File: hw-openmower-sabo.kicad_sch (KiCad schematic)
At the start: 20 parts, among them J1 Conn_01x05_Pin, J20 Conn_01x02, J31 Conn_01x03_Pin, J32 Conn_02x08_Odd_Even, J33 Molex 470531000, M1 Fan, M2 Fan, Q4 BSS138, Q5 BSS138, U7 M24C02-WMN

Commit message: Update status
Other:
- note added: "--------------- DESIGN FAULTS -------------- 1. Front-Wheel & Top- Stop-Button Emergencies for Series-I: Outputs of OPAMPs (for Series-II) need to get cutted! U6 Pin1, 2 & 14 2. See required changes in RobotConnectorsSeries2"
- note removed: "--------------- DESIGN FAILURES -------------- 1. Front-Wheel & Top- Stop-Button Emergencies for Series-I: Outputs of OPAMPs (for Series-II) need to get cutted! U6 Pin1, 2 & 14"
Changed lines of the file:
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@@
 		)
 	)
-	(text "--------------- DESIGN FAILURES --------------\n\n1. Front-Wheel & Top- Stop-Button Emergencies for Series-I:\n   Outputs of OPAMPs (for Series-II) need to get cutted!\n   U6 Pin1, 2 & 14"
+	(text "--------------- DESIGN FAULTS --------------\n\n1. Front-Wheel & Top- Stop-Button Emergencies for Series-I:\n   Outputs of OPAMPs (for Series-II) need to get cutted!\n   U6 Pin1, 2 & 14\n2. See required changes in RobotConnectorsSeries2"
 		(exclude_from_sim no)
 		(at 24.638 87.122 0)

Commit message: Prepare v0.2
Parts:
- added C88: 100nF@50V, Capacitor_SMD:C_0402_1005Metric, symbol Device:C
- added R36: 0.1, Resistor_SMD:R_1206_3216Metric, symbol Device:R
- added R37: 27k, Resistor_SMD:R_0603_1608Metric_Pad0.98x0.95mm_HandSolder, symbol Device:R
- added R38: 22k, Resistor_SMD:R_0603_1608Metric_Pad0.98x0.95mm_HandSolder, symbol Device:R
- added U44: INA180A1, Package_TO_SOT_SMD:SOT-23-5, symbol Amplifier_Current:INA180A1
- J20: now fitted; now in the parts list
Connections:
- net 3.3V: now also C88.1, U44.5 (V+)
- net AGPIO2: now also U44.1
- net GND: now also C88.2, R37.2, U44.2 (GND)
- net VIN: now also R36.2, U44.4 (-); no longer D15.1 (K), D28.1 (K)
- new net: R37.1, R38.1, U44.3 (+)
- new net: D15.1 (K), D28.1 (K), R36.1, R38.2
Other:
- sheet RobotConnectors ports: added INP_~{CS}, LATCH_~{LOAD}, SPI_CLK, SPI_RX, SPI_TX, UI_S2_BTN_~{CS}, ~{OE}; removed LED_RX, LED_TX, UI_BTN_~{CE}, UI_LATCH_LOAD, UI_SPI_CLK, UI_SPI_RX, UI_SPI_TX, UI_~{OE}
- note added: "(PA8)"
- note added: "(PF7)"
- note removed: "--------------- DESIGN FAULTS -------------- 1. Front-Wheel & Top- Stop-Button Emergencies for Series-I: Outputs of OPAMPs (for Series-II) need to get cutted! U6 Pin1, 2 & 14 2. See required changes in RobotConnectorsSeries2"
- moved on the sheet: D15, D28

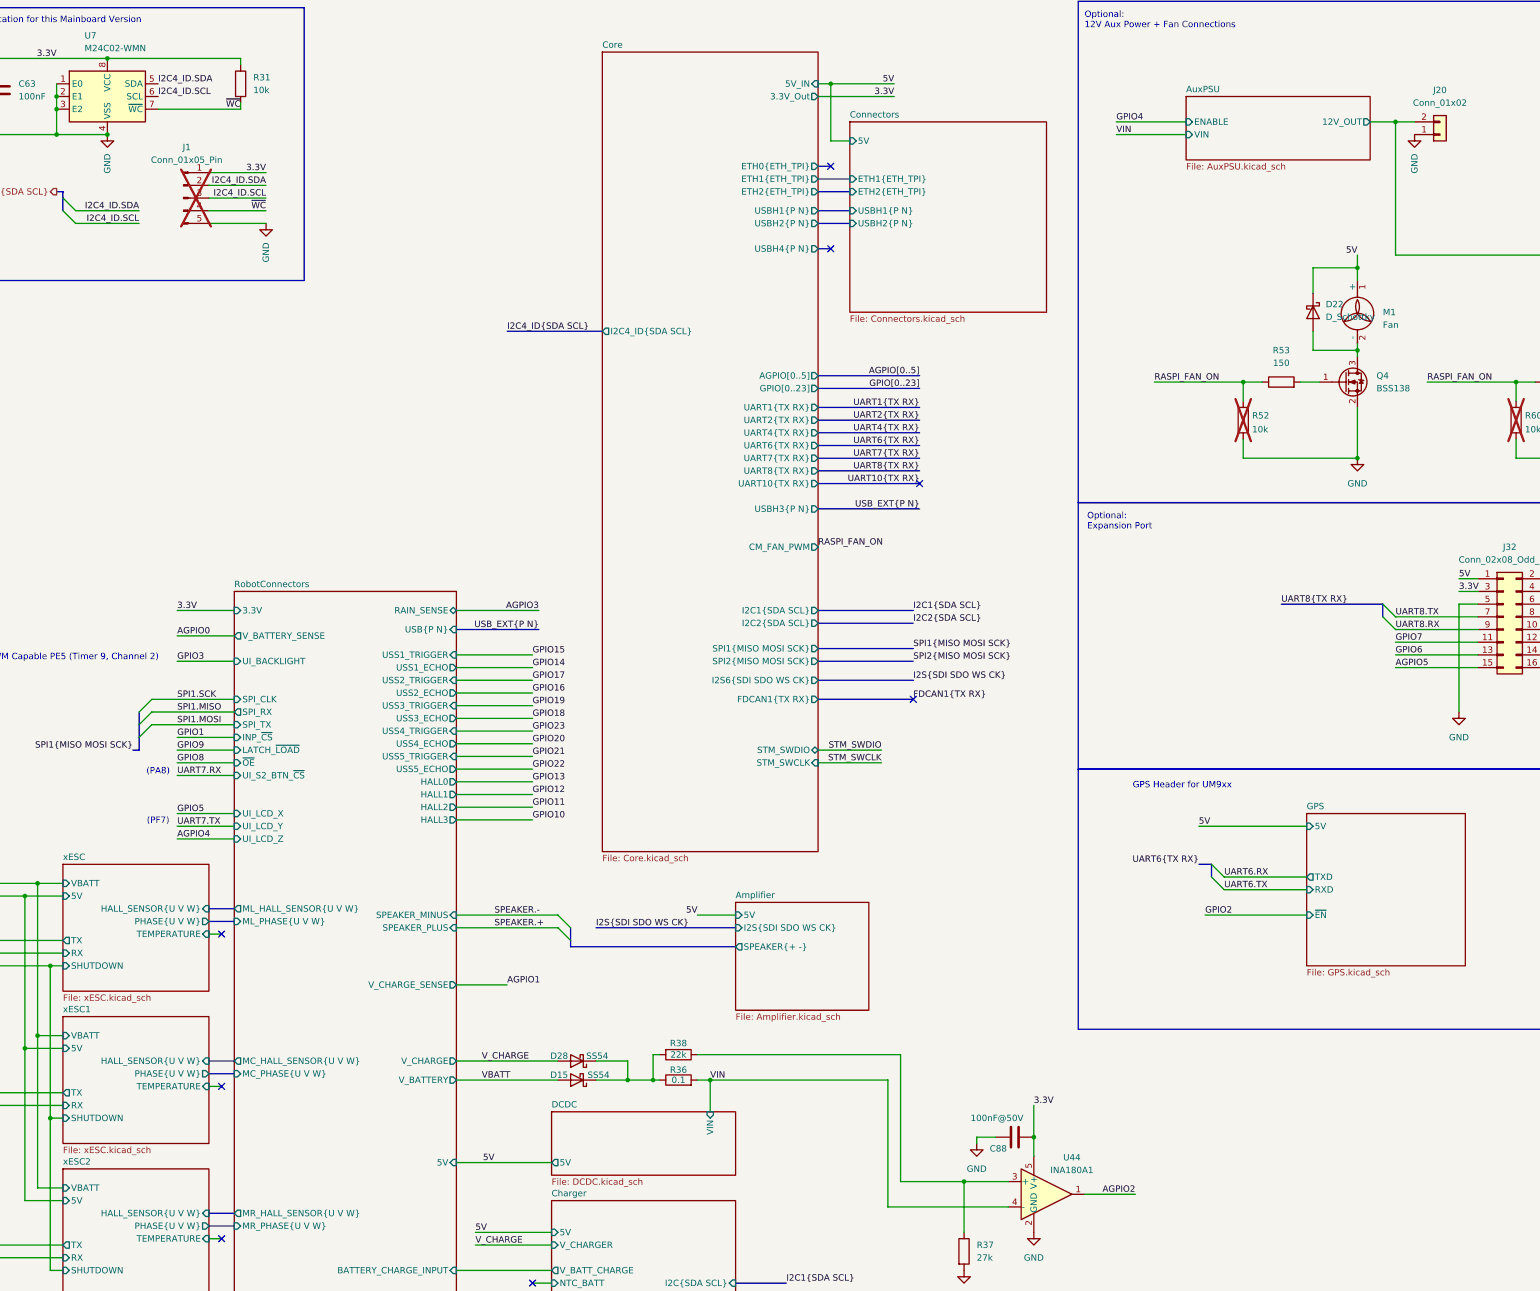
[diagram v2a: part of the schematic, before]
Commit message: Add RoHS Compliance Summary
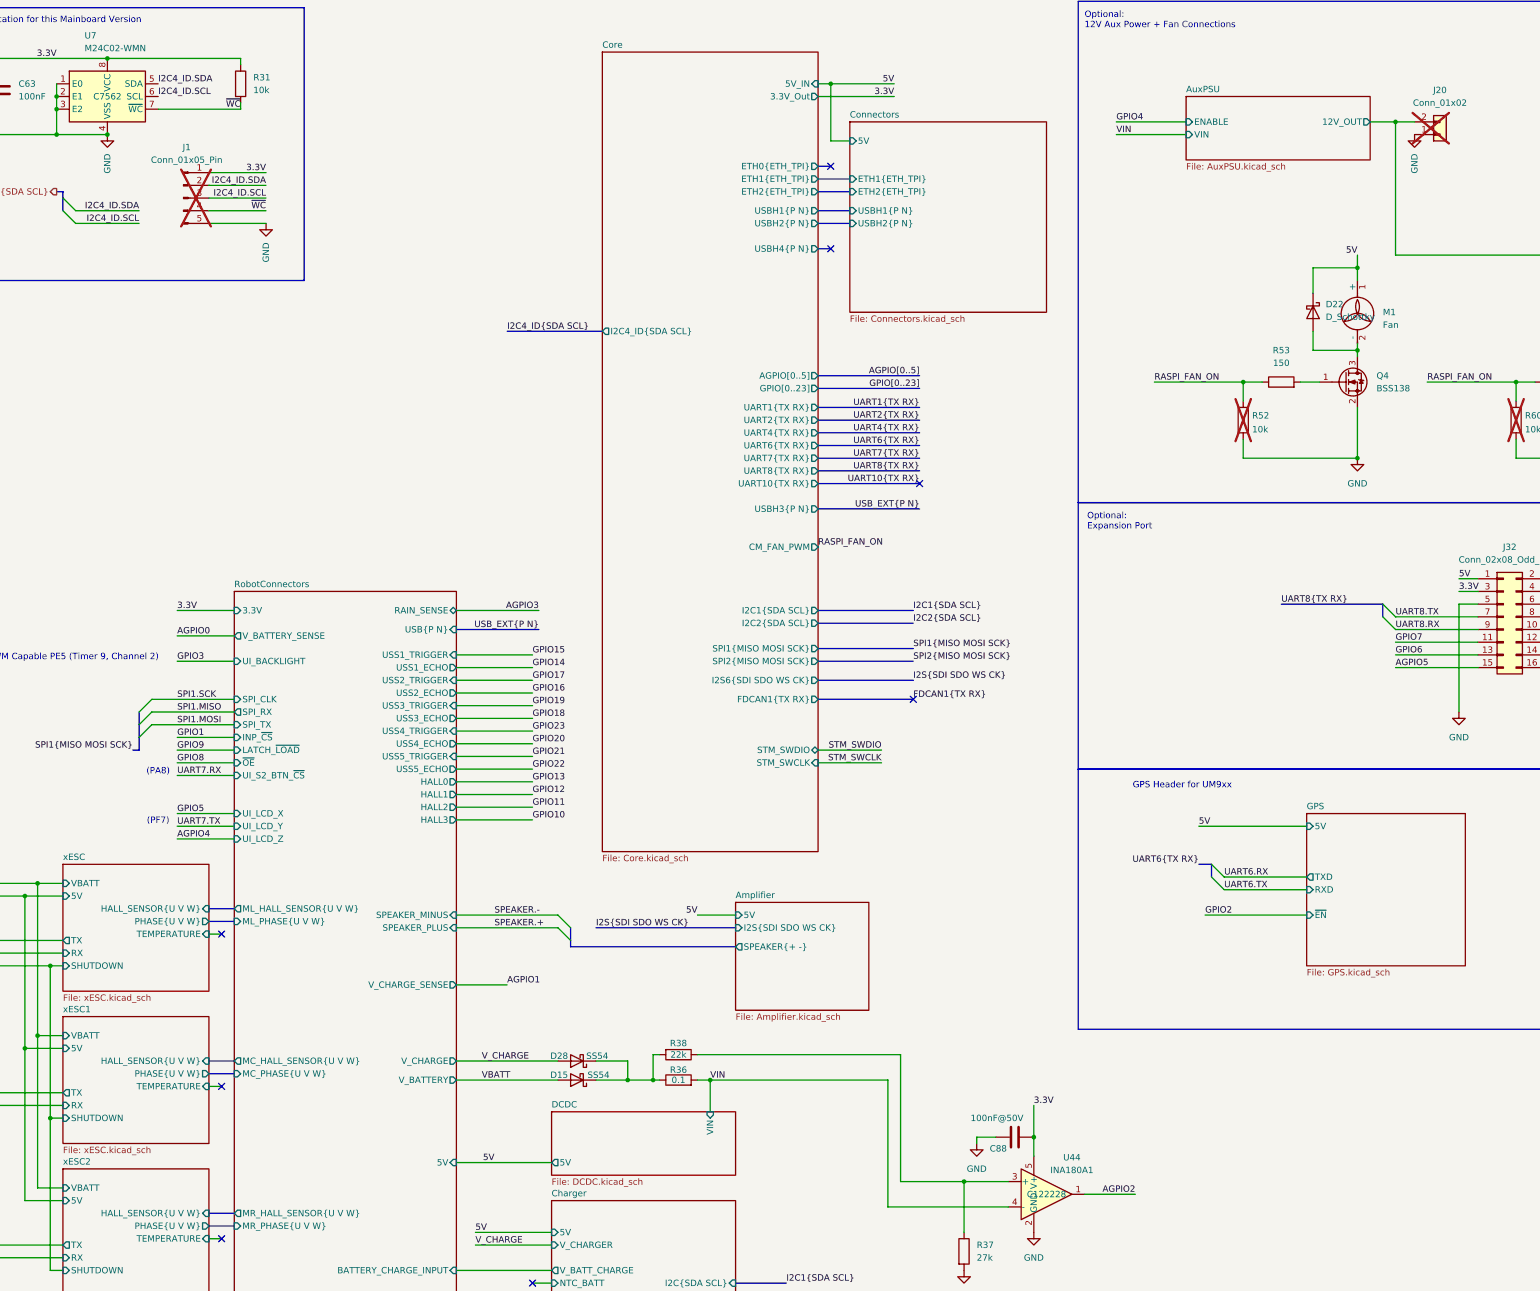
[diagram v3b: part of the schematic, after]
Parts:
- J20: now not fitted; now left out of the parts list
- U44: JLC C122228 -> (none); LCSC Part # (none) -> C122228
- U7: JLC C7562 -> (none); LCSC Part # (none) -> C7562
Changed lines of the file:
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@@
+			)
+		)
+		(property "MPN" ""
+			(at 161.29 224.79 0)
+			(effects
+				(font
+					(size 1.27 1.27)
+				)
 			)
 		)
@@
 			)
 		)
+		(property "MPN" ""
+			(at 326.39 137.16 0)
+			(effects
+				(font
+					(size 1.27 1.27)
+				)
+			)
+		)
 		(pin "9"
 		)
@@
 			)
 		)
+		(property "MPN" ""
+			(at 365.76 193.04 0)
+			(effects
+				(font
+					(size 1.27 1.27)
+				)
+			)
+		)
 		(pin "1"
 		)
@@
 			)
 		)
+		(property "MPN" ""
+			(at 351.79 77.47 0)
+			(effects
+				(font
+					(size 1.27 1.27)
+				)
+			)
+		)
 		(pin "1"
 		)
@@
 				)
 				(hide yes)
+			)
+		)
+		(property "MPN" ""
+			(at 140.97 226.06 0)
+			(effects
+				(font
+					(size 1.27 1.27)
+				)
 			)
 		)
@@
 			)
 		)
+		(property "MPN" ""
+			(at 349.25 90.17 0)
+			(effects
+				(font
+					(size 1.27 1.27)
+				)
+			)
+		)
 		(pin "1"
 		)
@@
 			)
 		)
+		(property "MPN" ""
+			(at 297.18 77.47 0)
+			(effects
+				(font
+					(size 1.27 1.27)
+				)
+			)
+		)
 		(pin "1"
 		)
@@
 			)
 		)
+		(property "MPN" ""
+			(at 274.32 97.79 0)
+			(effects
+				(font
+					(size 1.27 1.27)
+				)
+			)
+		)
 		(pin "1"
 		)
@@
 			)
 		)
+		(property "MPN" ""
+			(at 140.97 229.87 0)
+			(effects
+				(font
+					(size 1.27 1.27)
+				)
+			)
+		)
 		(pin "1"
 		)
@@
 			)
 		)
-		(property "JLC" "C7562"
+		(property "JLC" ""
 			(at 46.99 33.02 0)
 			(effects
@@
 				)
 				(hide yes)
+			)
+		)
+		(property "MPN" ""
+			(at 46.99 33.02 0)
+			(effects
+				(font
+					(size 1.27 1.27)
+				)
+			)
+		)
+		(property "LCSC Part #" "C7562"
+			(at 46.99 33.02 0)
+			(effects
+				(font
+					(size 1.27 1.27)
+				)
 			)
 		)
@@
 			)
 		)
+		(property "MPN" ""
+			(at 294.64 90.17 0)
+			(effects
+				(font
+					(size 1.27 1.27)
+				)
+			)
+		)
 		(pin "1"
 		)
@@
 			)
 		)
+		(property "MPN" ""
+			(at 73.66 30.48 0)
+			(effects
+				(font
+					(size 1.27 1.27)
+				)
+			)
+		)
 		(pin "2"
 		)
@@
 			)
 		)
-		(property "JLC" "C122228"
+		(property "JLC" ""
 			(at 234.95 252.73 0)
 			(effects
@@
 				)
 				(hide yes)
+			)
+		)
+		(property "MPN" ""
+			(at 234.95 252.73 0)
+			(effects
+				(font
+					(size 1.27 1.27)
+				)
+			)
+		)
+		(property "LCSC Part #" "C122228"
+			(at 234.95 252.73 0)
+			(effects
+				(font
+					(size 1.27 1.27)
+				)
 			)
 		)
@@
 			)
 		)
+		(property "MPN" ""
+			(at 218.44 264.16 0)
+			(effects
+				(font
+					(size 1.27 1.27)
+				)
+			)
+		)
 		(pin "2"
 		)
@@
 			)
 		)
+		(property "MPN" ""
+			(at 62.23 53.34 0)
+			(effects
+				(font
+					(size 1.27 1.27)
+				)
+			)
+		)
 		(pin "5"
 		)
@@
 			)
 		)
+		(property "MPN" ""
+			(at 342.9 76.2 0)
+			(effects
+				(font
+					(size 1.27 1.27)
+				)
+			)
+		)
 		(pin "1"
 		)
@@
 			)
 		)
+		(property "MPN" ""
+			(at 281.94 90.17 0)
+			(effects
+				(font
+					(size 1.27 1.27)
+				)
+			)
+		)
 		(pin "1"
 		)
@@
 			)
 		)
+		(property "MPN" ""
+			(at 336.55 90.17 0)
+			(effects
+				(font
+					(size 1.27 1.27)
+				)
+			)
+		)
 		(pin "1"
 		)
@@
 			)
 		)
+		(property "MPN" ""
+			(at 161.29 229.87 0)
+			(effects
+				(font
+					(size 1.27 1.27)
+				)
+			)
+		)
 		(pin "2"
 		)
@@
 		(unit 1)
 		(exclude_from_sim no)
-		(in_bom yes)
-		(on_board yes)
-		(dnp no)
+		(in_bom no)
+		(on_board yes)
+		(dnp yes)
 		(property "Reference" "J20"
 			(at 313.69 31.75 0)
@@
 				)
 				(hide yes)
+			)
+		)
+		(property "MPN" ""
+			(at 313.69 40.64 0)
+			(effects
+				(font
+					(size 1.27 1.27)
+				)
 			)
 		)
@@
 			)
 		)
+		(property "MPN" ""
+			(at 328.93 97.79 0)
+			(effects
+				(font
+					(size 1.27 1.27)
+				)
+			)
+		)
 		(pin "1"
 		)
@@
 			)
 		)
+		(property "MPN" ""
+			(at 288.29 76.2 0)
+			(effects
+				(font
+					(size 1.27 1.27)
+				)
+			)
+		)
 		(pin "1"
 		)
@@
 			)
 		)
+		(property "MPN" ""
+			(at 386.08 91.44 0)
+			(effects
+				(font
+					(size 1.27 1.27)
+				)
+			)
+		)
 		(pin "1"
 		)
@@
 				)
 				(hide yes)
+			)
+		)
+		(property "MPN" ""
+			(at 228.6 241.3 0)
+			(effects
+				(font
+					(size 1.27 1.27)
+				)
 			)
 		)
@@
 			)
 		)
+		(property "MPN" ""
+			(at 25.4 31.75 0)
+			(effects
+				(font
+					(size 1.27 1.27)
+				)
+			)
+		)

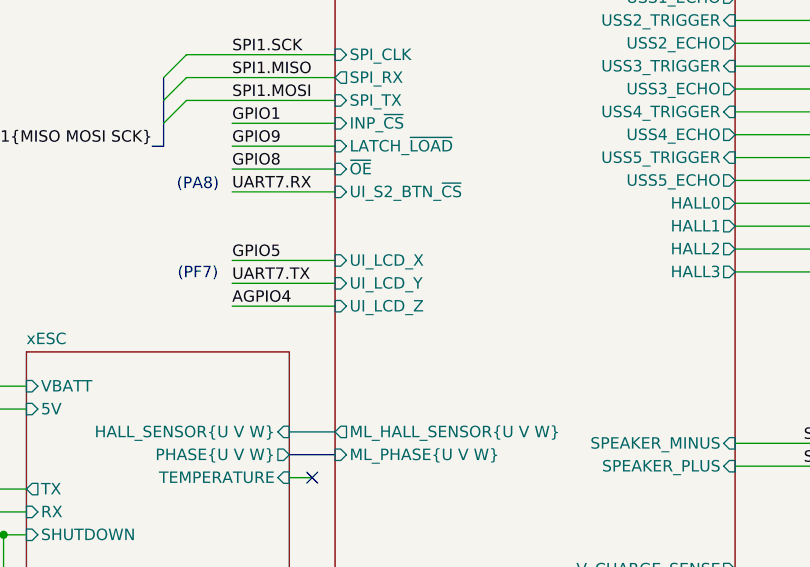
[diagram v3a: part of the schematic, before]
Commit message: Finish v0.2 schematic and ERC
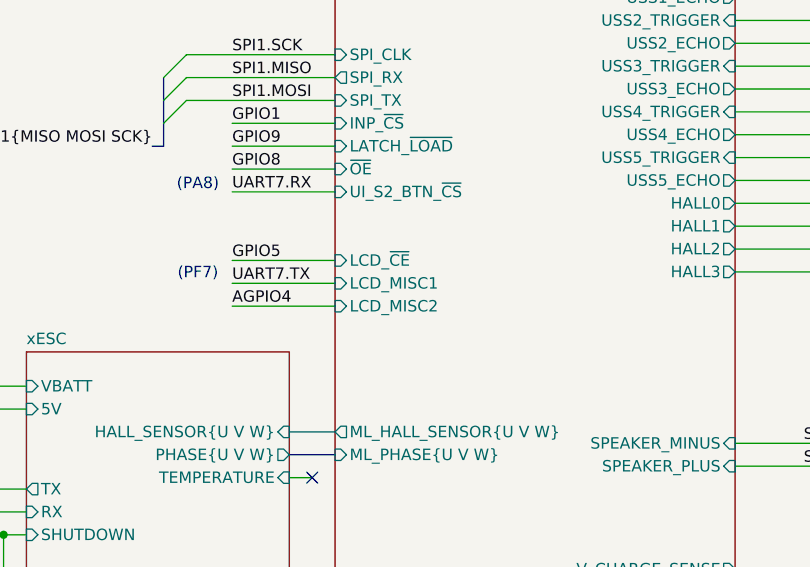
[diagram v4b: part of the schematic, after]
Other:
- sheet RobotConnectors ports: added LCD_MISC1, LCD_MISC2, LCD_~{CE}; removed UI_LCD_X, UI_LCD_Y, UI_LCD_Z
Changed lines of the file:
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@@
 	(title_block
 		(title "OpenMower SABO Mainboard for Series I & II")
-		(date "2025-05-04")
+		(date "2025-05-22")
 		(rev "v0.2")
 		(company "Apeheanger <joerg@ebeling.ws> for OpenMower")
@@
 			)
 		)
-		(pin "UI_LCD_X" input
-			(at 72.39 176.53 180)
+		(pin "UI_S2_BTN_~{CS}" input
+			(at 72.39 168.91 180)
 			(effects
 				(font
@@
 			)
 		)
-		(pin "UI_LCD_Y" input
+		(pin "LCD_MISC1" input
 			(at 72.39 179.07 180)
 			(effects
@@
 			)
 		)
-		(pin "UI_LCD_Z" input
+		(pin "LCD_MISC2" input
 			(at 72.39 181.61 180)
 			(effects
@@
 			)
 		)
-		(pin "UI_S2_BTN_~{CS}" input
-			(at 72.39 168.91 180)
+		(pin "LCD_~{CE}" input
+			(at 72.39 176.53 180)
 			(effects
 				(font

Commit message: Finish v0.2 PCB and DRC
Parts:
- J32: JLC C779499 -> C5383108
- J33: JLC C240840 -> C2761402
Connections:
- net 3.3V renamed +3V3

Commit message: Additional Infos
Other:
- note added: "--------------- DESIGN FAULTS -------------- 1. See required changes in RobotConnectors"
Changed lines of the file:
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@@
+		)
+	)
+	(text "--------------- DESIGN FAULTS --------------\n\n1. See required changes in RobotConnectors"
+		(exclude_from_sim no)
+		(at 26.162 95.25 0)
+		(effects
+			(font
+				(size 1.778 1.778)
+				(thickness 0.254)
+				(bold yes)
+				(color 255 0 0 1)
+			)
+			(justify left)
 		)
 	)

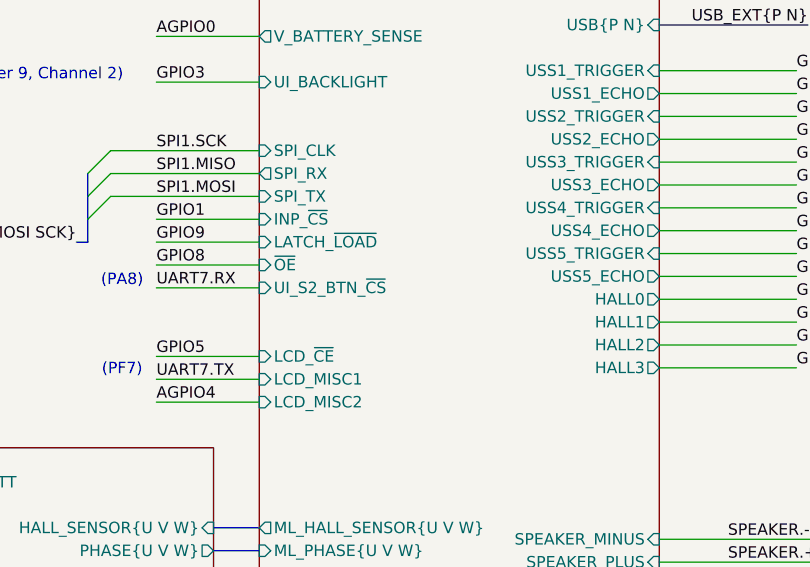
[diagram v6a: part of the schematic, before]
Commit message: Update state and required v0.2 PCB modifications
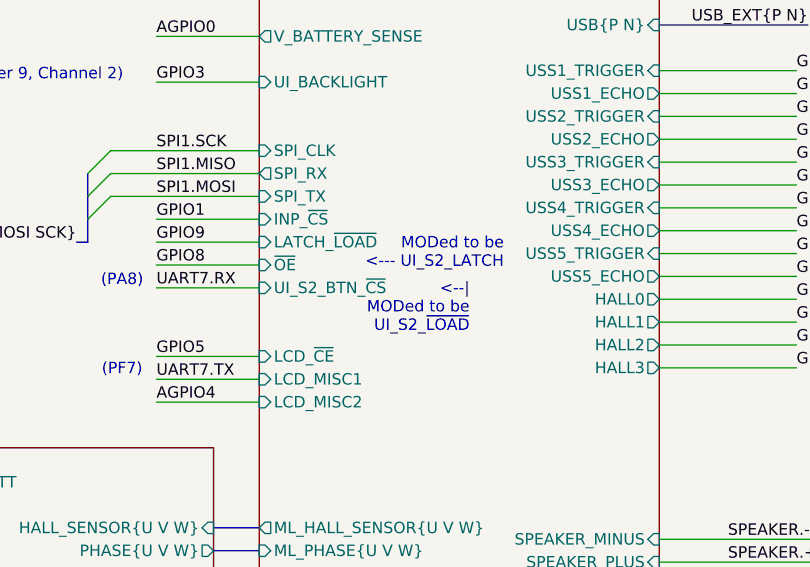
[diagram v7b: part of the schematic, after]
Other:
- note added: "<--| MODed to be UI_S2_~{LOAD}"
- note added: "MODed to be <--- UI_S2_LATCH"
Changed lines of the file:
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@@
 		)
 	)
+	(text "<--|\nMODed to be\nUI_S2_~{LOAD}"
+		(exclude_from_sim no)
+		(at 95.758 171.196 0)
+		(effects
+			(font
+				(size 1.27 1.27)
+				(color 2 142 4 1)
+			)
+			(justify right)
+		)
+	)
+	(text "MODed to be\n<--- UI_S2_LATCH"
+		(exclude_from_sim no)
+		(at 99.568 165.1 0)
+		(effects
+			(font
+				(size 1.27 1.27)
+				(color 2 142 4 1)
+			)
+			(justify right)
+		)
+	)
 	(junction
 		(at 46.99 25.4)
@@
 				(font
 					(size 1.27 1.27)
+					(color 255 0 3 1)
 				)
 				(justify left)

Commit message: v0.2 required changes
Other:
- sheet RobotConnectors ports: added LCD_~{C}D, LCD_~{RST}; removed LCD_MISC1, LCD_MISC2
- note added: "----- REQUIRED REWORK ----- 1. See RobotConnectors"
- note removed: "--------------- DESIGN FAULTS -------------- 1. See required changes in RobotConnectors"
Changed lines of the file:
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@@
 		)
 	)
-	(text "--------------- DESIGN FAULTS --------------\n\n1. See required changes in RobotConnectors"
+	(text "----- REQUIRED REWORK -----\n\n1. See RobotConnectors"
 		(exclude_from_sim no)
-		(at 26.162 95.25 0)
+		(at 36.322 92.71 0)
 		(effects
 			(font
-				(size 1.778 1.778)
+				(size 2.032 2.032)
 				(thickness 0.254)
 				(bold yes)
@@
 			)
 		)
-		(pin "LCD_MISC1" input
+		(pin "LCD_~{RST}" input
 			(at 72.39 179.07 180)
 			(effects
@@
 			)
 		)
-		(pin "LCD_MISC2" input
+		(pin "LCD_~{C}D" input
 			(at 72.39 181.61 180)
 			(effects
